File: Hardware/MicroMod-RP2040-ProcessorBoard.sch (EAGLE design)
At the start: 36 parts, among them J1 MICROMOD-2222, U1 W25QXX128MBIT, U3 RP2040, Y1 12MHz

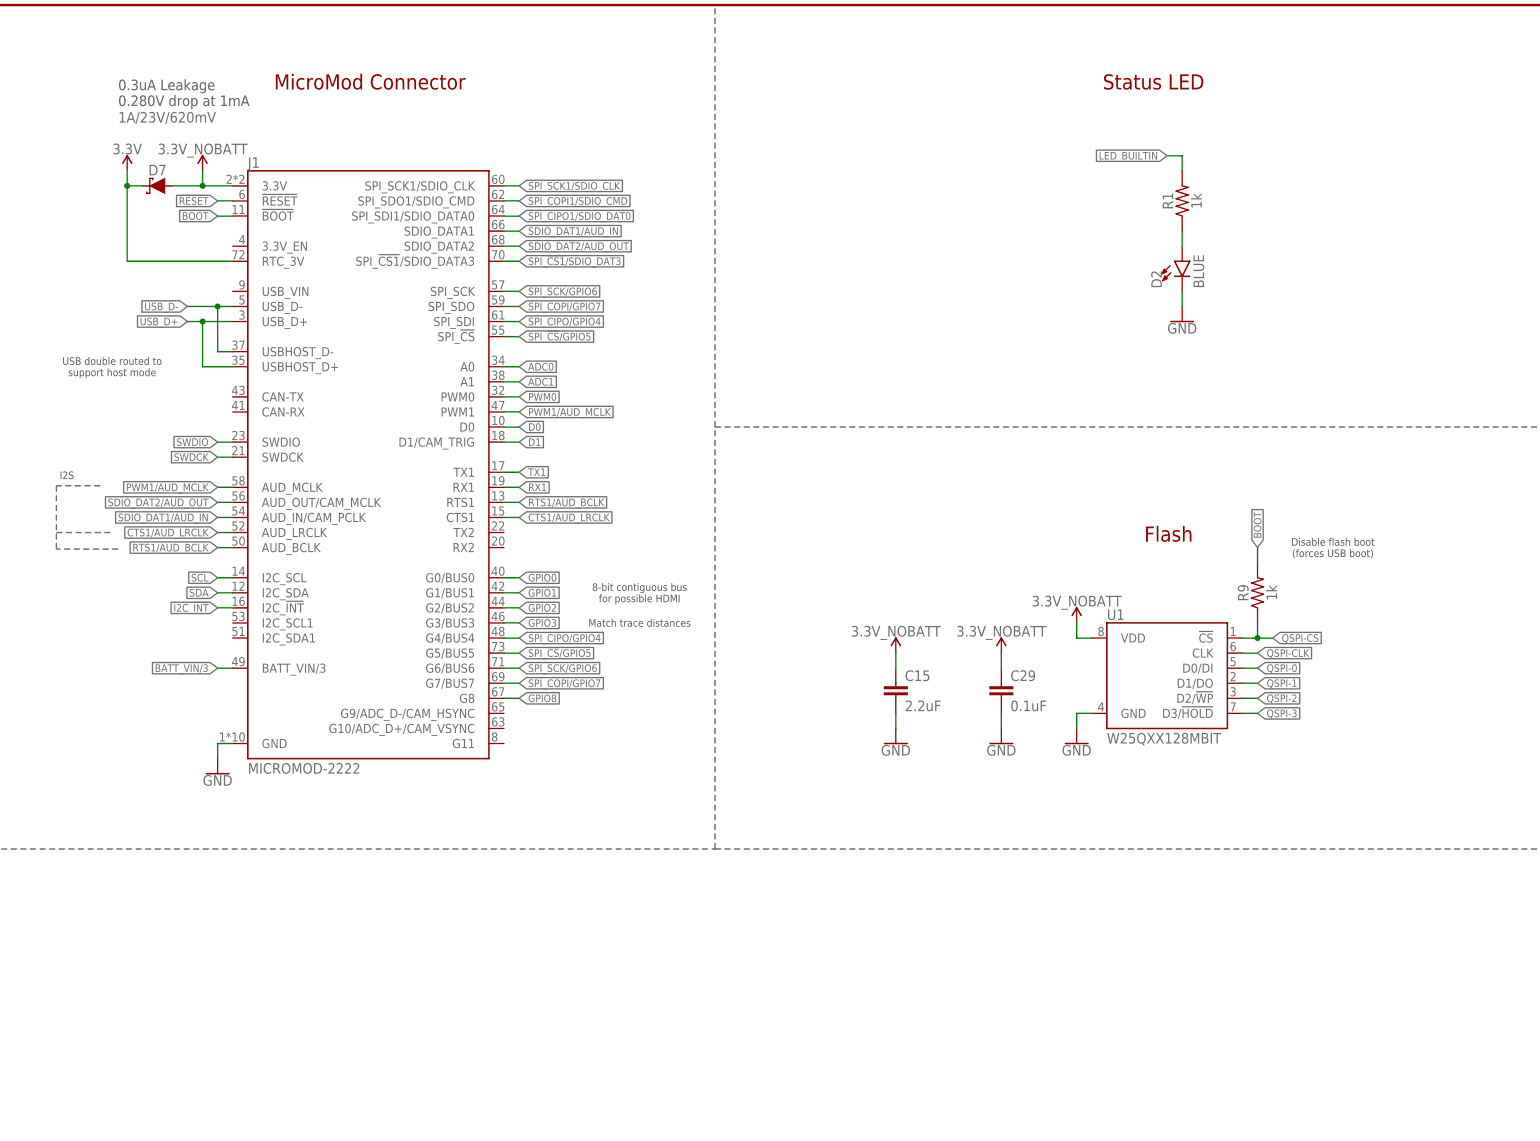
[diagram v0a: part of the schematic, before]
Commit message: Add pullup to flash
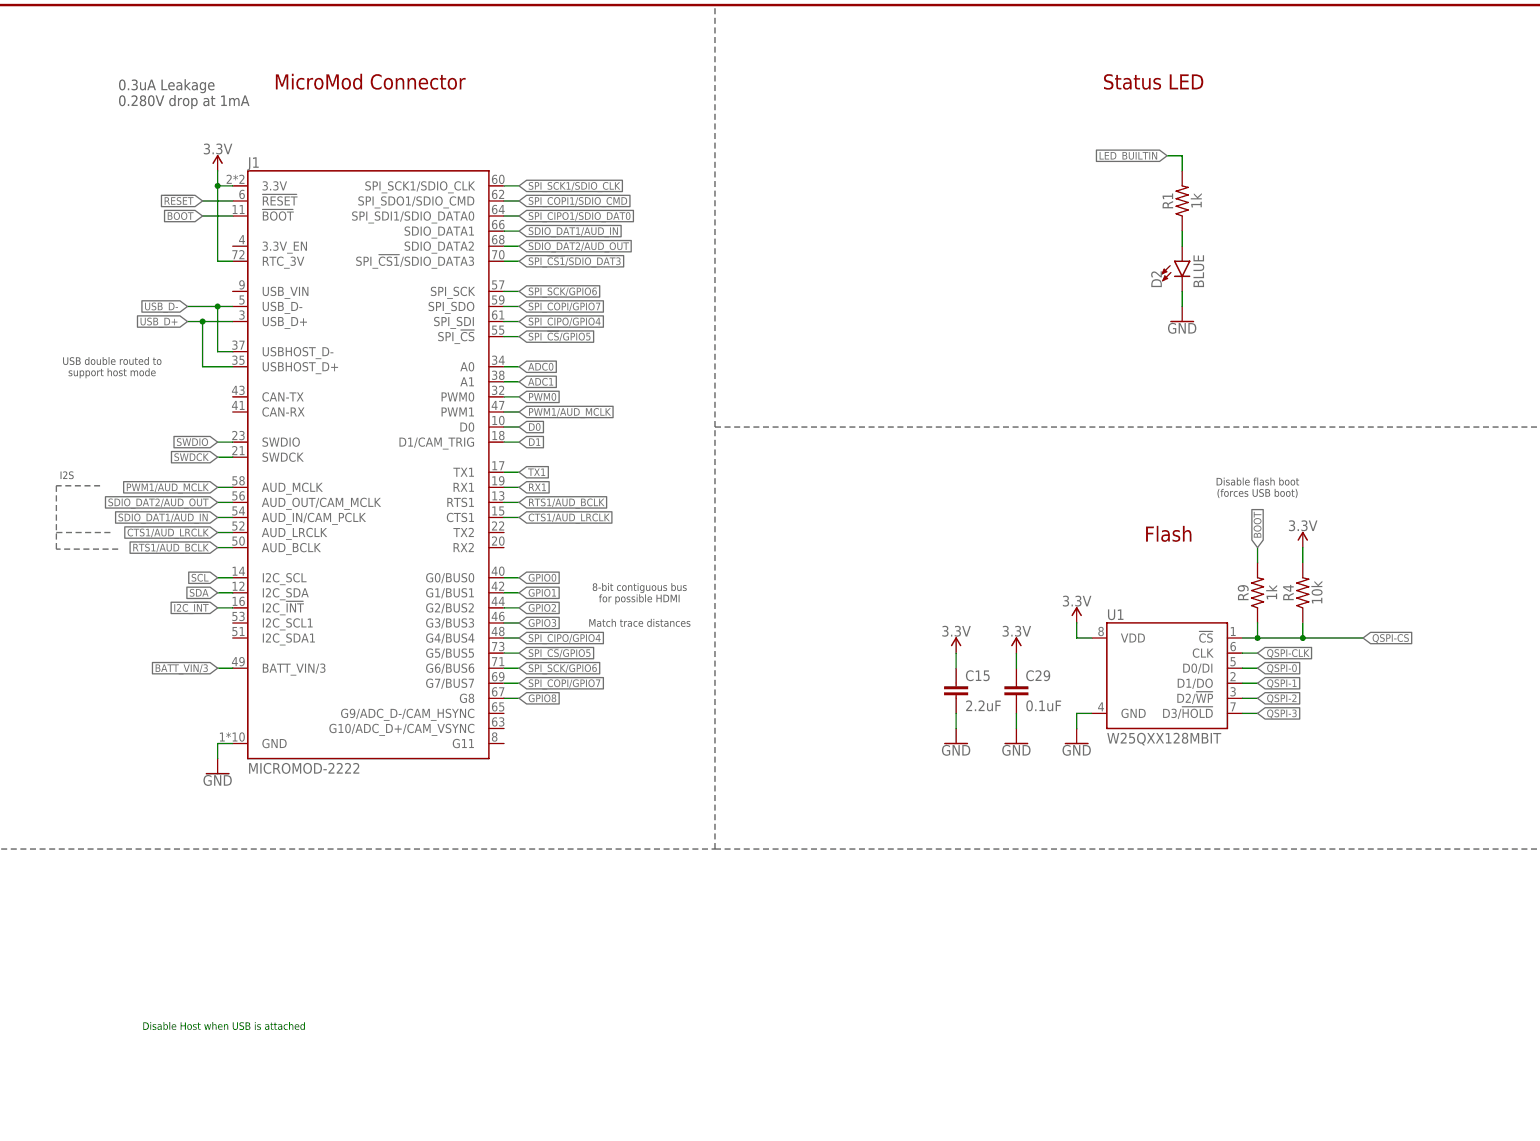
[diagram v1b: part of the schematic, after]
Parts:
- removed D7: 1A/23V/620mV, SparkFun-DiscreteSemi:DIODE-SCHOTTKY-BAT20J
- added R4: 10k, SparkFun-Resistors:10KOHM-0402T-1/16W-1%
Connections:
- removed net 3.3V_NOBATT: C15.1, C29.1, D7.A, J1.3.3V, U1.VDD
- net 3.3V: now also C15.1, C29.1, J1.3.3V, R4.2, U1.VDD; no longer D7.C
- net QSPI-CS: now also R4.1
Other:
- note added: "Disable Host when USB is attached"
- moved on the sheet: C15, C29

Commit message: Adding production files
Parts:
- added C2: 0.1uF, SparkFun-Capacitors:0.1UF-0402T-6.3V-10%-X7R
- added R18: 1k, SparkFun-Resistors:1KOHM-0402T-1/16W-1%
- added R5: 10k, SparkFun-Resistors:10KOHM-0402T-1/16W-1%
- added U2: FSUSB30MUX_MSOP10, RP2040:FSUSB30MUX_MSOP10
- R2: value 200 -> 200OHM-0402T-1/16W-1%; device SparkFun-Resistors:200OHM-0603-1/10W-1% -> SparkFun-Resistors:200OHM-0402T-1/16W-1%
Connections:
- net N$1 renamed RP_D1-
- net N$3 renamed ADC_VDD
- net N$7 renamed RP_D1+
- removed net GPIO8: J1.G8, U3.GPIO28/ADC2
- removed net I2C_!INT!: J1.I2C_!INT!, U3.GPIO13
- removed net LED_BUILTIN: R1.2, U3.GPIO25
- removed net SPI_!CS1!/SDIO_DAT3: J1.SPI_!CS1!/SDIO_DATA3, U3.GPIO9
- new net GPIO9: J1.G9/ADC_D-/CAM_HSYNC, U3.GPIO28/ADC2
- new net I2C_!INT!/TX2: J1.I2C_!INT!, J1.TX2, U3.GPIO8
- new net LED_BUILTIN/G10: J1.G10/ADC_D+/CAM_VSYNC, R1.2, U3.GPIO25
- new net RP_D+: R10.1, U2.D+
- new net RP_D-: R11.1, U2.D-
- new net SPI_!CS1!/SDIO_DAT3/RX2: J1.RX2, J1.SPI_!CS1!/SDIO_DATA3, U3.GPIO9
- new net USBHOST_D+: J1.USBHOST_D+, U2.D1+
- new net USBHOST_D-: J1.USBHOST_D-, U2.D1-
- new net USB_MUX_SIG: R18.2, R5.2, U2.S
- new net USB_VIN: J1.USB_VIN, R18.1
- net 3.3V: now also C2.1, U2.VCC
- net GND: now also C2.2, R5.1, U2.!OE!, U2.GND
- net PWM0: now also U3.GPIO13; no longer U3.GPIO8
- net USB_D+: now also U2.D2+; no longer J1.USBHOST_D+, R10.1
- net USB_D-: now also U2.D2-; no longer J1.USBHOST_D-, R11.1
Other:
- note added: "16MB Flash"
- note added: "Board thickness: 0.8mm"
- note added: "Dielectric thickness (layer 1 to 2): 3.93mil/0.1mm"
- note added: "Differential Impedance: 100Ω"
- note added: "Differential Microstrip Calculation:"
- note added: "Er: 4.6 (JLC7628)"
- note added: "Matched length"
- note added: "RP2040 connected to D2/USB when USB_VIN detected. RP2040 connected to D1/USB_HOST otherwise."
- note added: "Required Trace Separation: 4mil"
- note added: "Required Trace Width: 5mil"
- note added: "Single Ended Impedance: 50Ω"
- note added: "Trace Thickness (1oz): 1.4mil/0.035mm"
- note added: "USB Mux"
- note added: "https://cart.jlcpcb.com/impedanceCalculation"
- note removed: "Disable Host when USB is attached"
- note removed: "Flash"
- note removed: "Match trace distances"
- note removed: "USB double routed to support host mode"
- moved on the sheet: C15, C29, D2, R1, R4, R9, U1

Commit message: Update USB mux prod ID
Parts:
- U2: device RP2040:FSUSB30MUX_MSOP10 -> SparkFun-IC-Special-Function:FSUSB30MUX_MSOP10
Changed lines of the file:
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@@
 <part name="SUPPLY5" library="SparkFun-PowerSymbols" deviceset="3.3V" device=""/>
 <part name="SUPPLY20" library="SparkFun-PowerSymbols" deviceset="3.3V" device=""/>
-<part name="U2" library="RP2040" deviceset="FSUSB30MUX" device="_MSOP10"/>
+<part name="U2" library="SparkFun-IC-Special-Function" deviceset="FSUSB30MUX" device="_MSOP10"/>
 <part name="SUPPLY2" library="SparkFun-PowerSymbols" deviceset="3.3V" device=""/>
 <part name="GND5" library="SparkFun-PowerSymbols" deviceset="GND" device=""/>

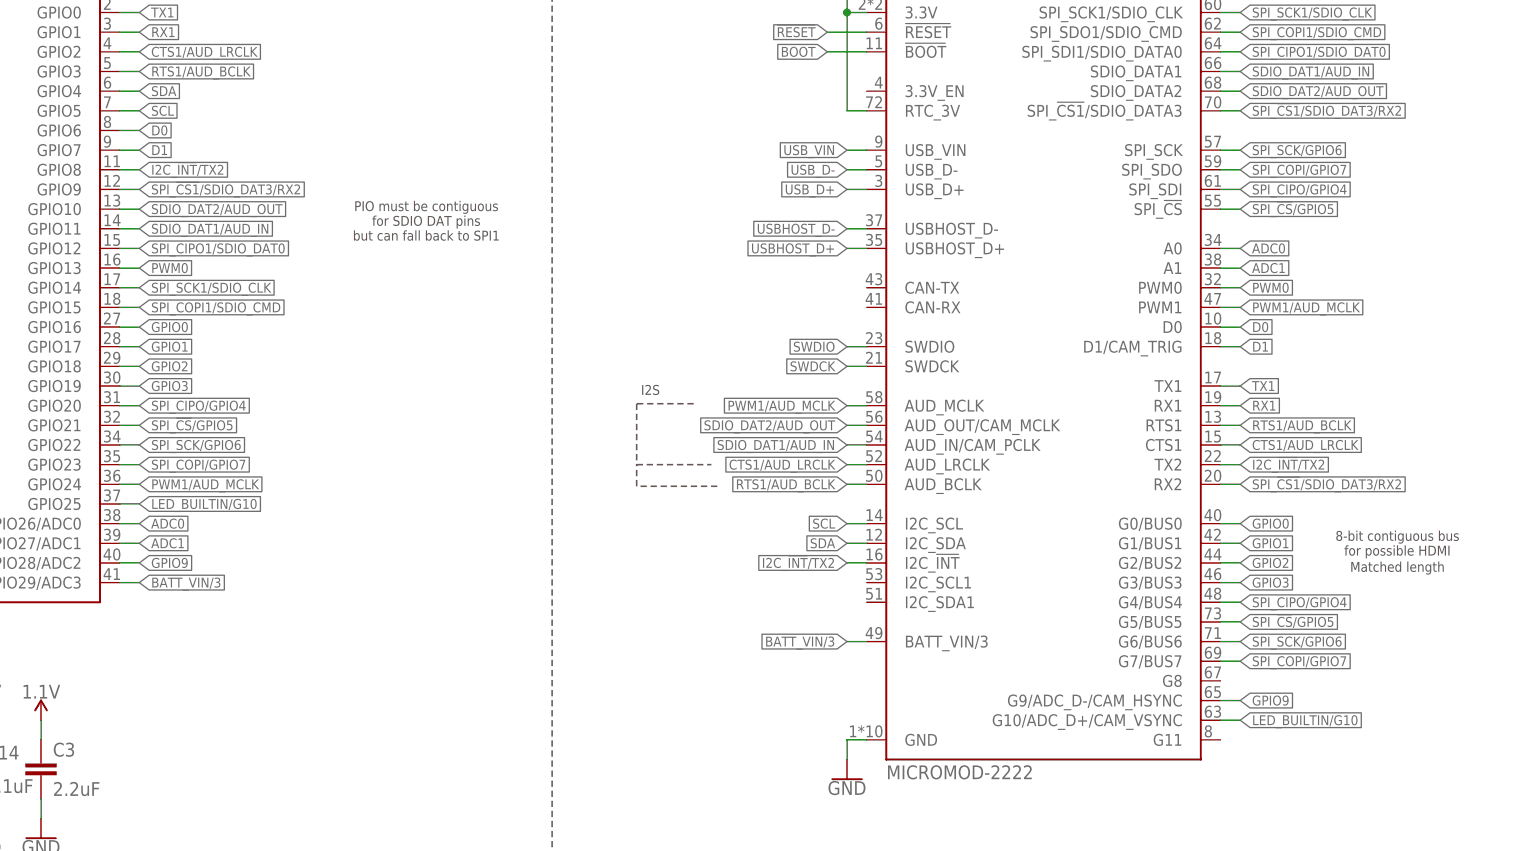
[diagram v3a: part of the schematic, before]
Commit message: Rename nets to match MicroMod nomenclature
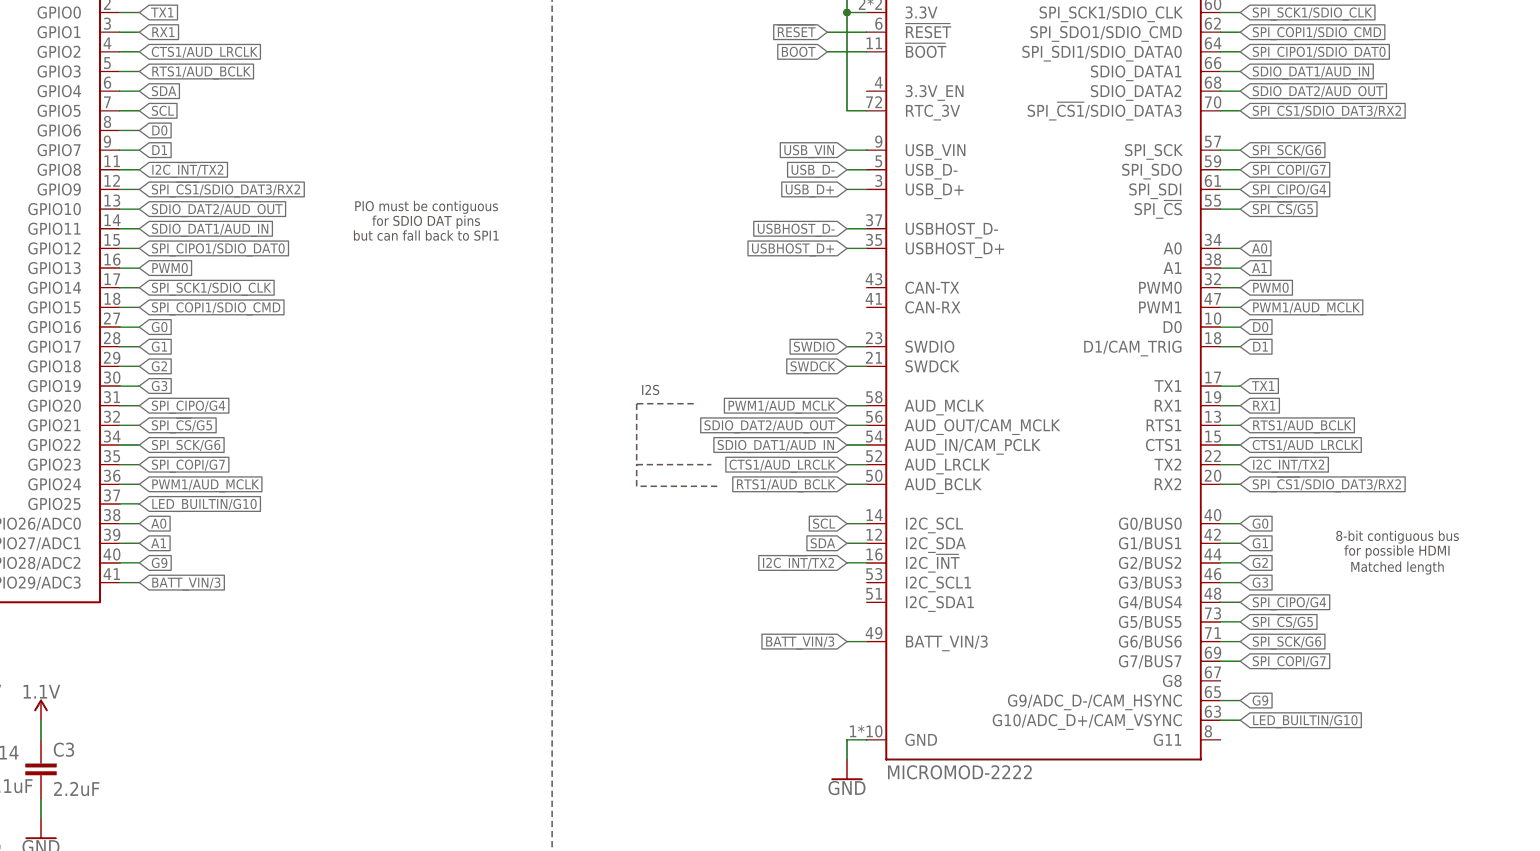
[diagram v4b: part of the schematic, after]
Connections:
- net ADC0 renamed A0
- net ADC1 renamed A1
- net GPIO0 renamed G0
- net GPIO1 renamed G1
- net GPIO2 renamed G2
- net GPIO3 renamed G3
- net GPIO9 renamed G9
- net SPI_!CS!/GPIO5 renamed SPI_!CS!/G5
- net SPI_CIPO/GPIO4 renamed SPI_CIPO/G4
- net SPI_COPI/GPIO7 renamed SPI_COPI/G7
- net SPI_SCK/GPIO6 renamed SPI_SCK/G6
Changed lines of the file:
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@@
 </segment>
 </net>
-<net name="SPI_SCK/GPIO6" class="1">
+<net name="SPI_SCK/G6" class="1">
 <segment>
 <wire x1="236.22" y1="231.14" x2="238.76" y2="231.14" width="0.1524" layer="91"/>
@@
 </segment>
 </net>
-<net name="SPI_COPI/GPIO7" class="1">
+<net name="SPI_COPI/G7" class="1">
 <segment>
 <wire x1="236.22" y1="228.6" x2="238.76" y2="228.6" width="0.1524" layer="91"/>
@@
 </segment>
 </net>
-<net name="ADC0" class="0">
+<net name="A0" class="0">
 <segment>
 <wire x1="236.22" y1="218.44" x2="238.76" y2="218.44" width="0.1524" layer="91"/>
@@
 </segment>
 </net>
-<net name="ADC1" class="0">
+<net name="A1" class="0">
 <segment>
 <wire x1="236.22" y1="215.9" x2="238.76" y2="215.9" width="0.1524" layer="91"/>
@@
 </segment>
 </net>
-<net name="SPI_CIPO/GPIO4" class="1">
+<net name="SPI_CIPO/G4" class="1">
 <segment>
 <wire x1="236.22" y1="226.06" x2="238.76" y2="226.06" width="0.1524" layer="91"/>
@@
 </segment>
 </net>
-<net name="SPI_!CS!/GPIO5" class="1">
+<net name="SPI_!CS!/G5" class="1">
 <segment>
 <pinref part="J1" gate="J1" pin="SPI_!CS!"/>
@@
 </segment>
 </net>
-<net name="GPIO1" class="1">
+<net name="G1" class="1">
 <segment>
 <wire x1="236.22" y1="180.34" x2="238.76" y2="180.34" width="0.1524" layer="91"/>
@@
 </segment>
 </net>
-<net name="GPIO3" class="1">
+<net name="G3" class="1">
 <segment>
 <wire x1="236.22" y1="175.26" x2="238.76" y2="175.26" width="0.1524" layer="91"/>
@@
 </segment>
 </net>
-<net name="GPIO2" class="1">
+<net name="G2" class="1">
 <segment>
 <wire x1="236.22" y1="177.8" x2="238.76" y2="177.8" width="0.1524" layer="91"/>
@@
 </segment>
 </net>
-<net name="GPIO0" class="1">
+<net name="G0" class="1">
 <segment>
 <wire x1="236.22" y1="182.88" x2="238.76" y2="182.88" width="0.1524" layer="91"/>
@@
 </segment>
 </net>
-<net name="GPIO9" class="0">
+<net name="G9" class="0">
 <segment>
 <pinref part="J1" gate="J1" pin="G9/ADC_D-/CAM_HSYNC"/>
